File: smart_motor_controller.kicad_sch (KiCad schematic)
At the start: 35 parts, among them J10 USB_B_Micro, J101 Breakout, J102 I2C_CONN, J103 CAN_CONN, J104 Debug, J9 Input 12V, SW102 SW_NRST, SW103 SW_NRST, U2 STM32F405RGT6, U3 USBLC6-2SC6

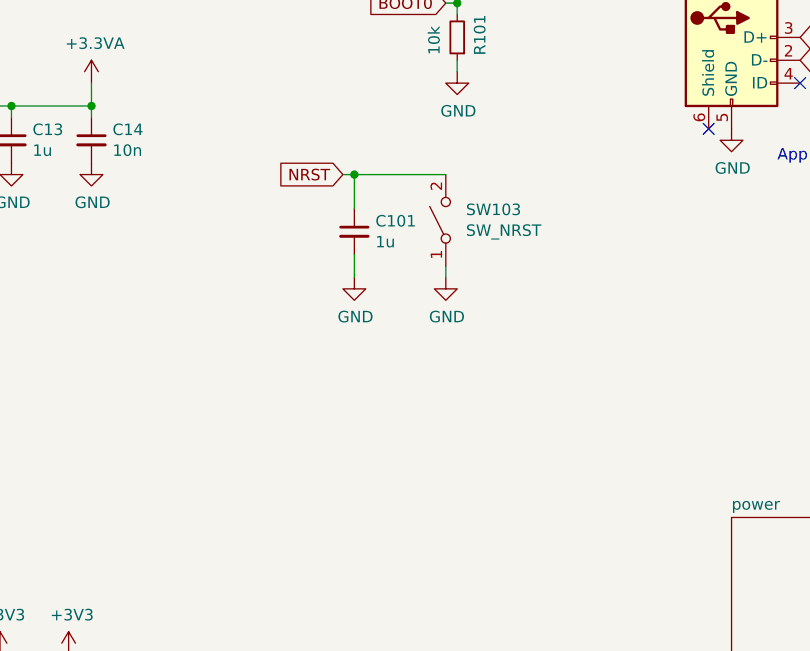
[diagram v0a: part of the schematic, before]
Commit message: Change components to 0603
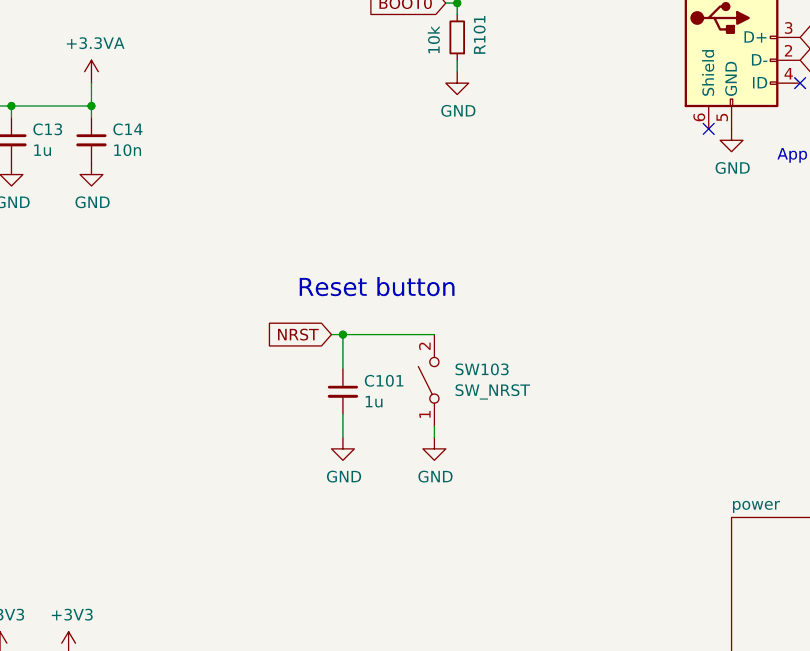
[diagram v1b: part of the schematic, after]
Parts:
- C101, C13, C14, C17, C18, C5, C6, C7, C8: footprint Capacitor_SMD:C_0402_1005Metric -> Capacitor_SMD:C_0603_1608Metric
- L2: footprint Inductor_SMD:L_0402_1005Metric -> Inductor_SMD:L_0603_1608Metric
- R101, R14, R15, R6: footprint Resistor_SMD:R_0402_1005Metric -> Resistor_SMD:R_0603_1608Metric
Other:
- note added: "Reset button"
- moved on the sheet: C101, SW103

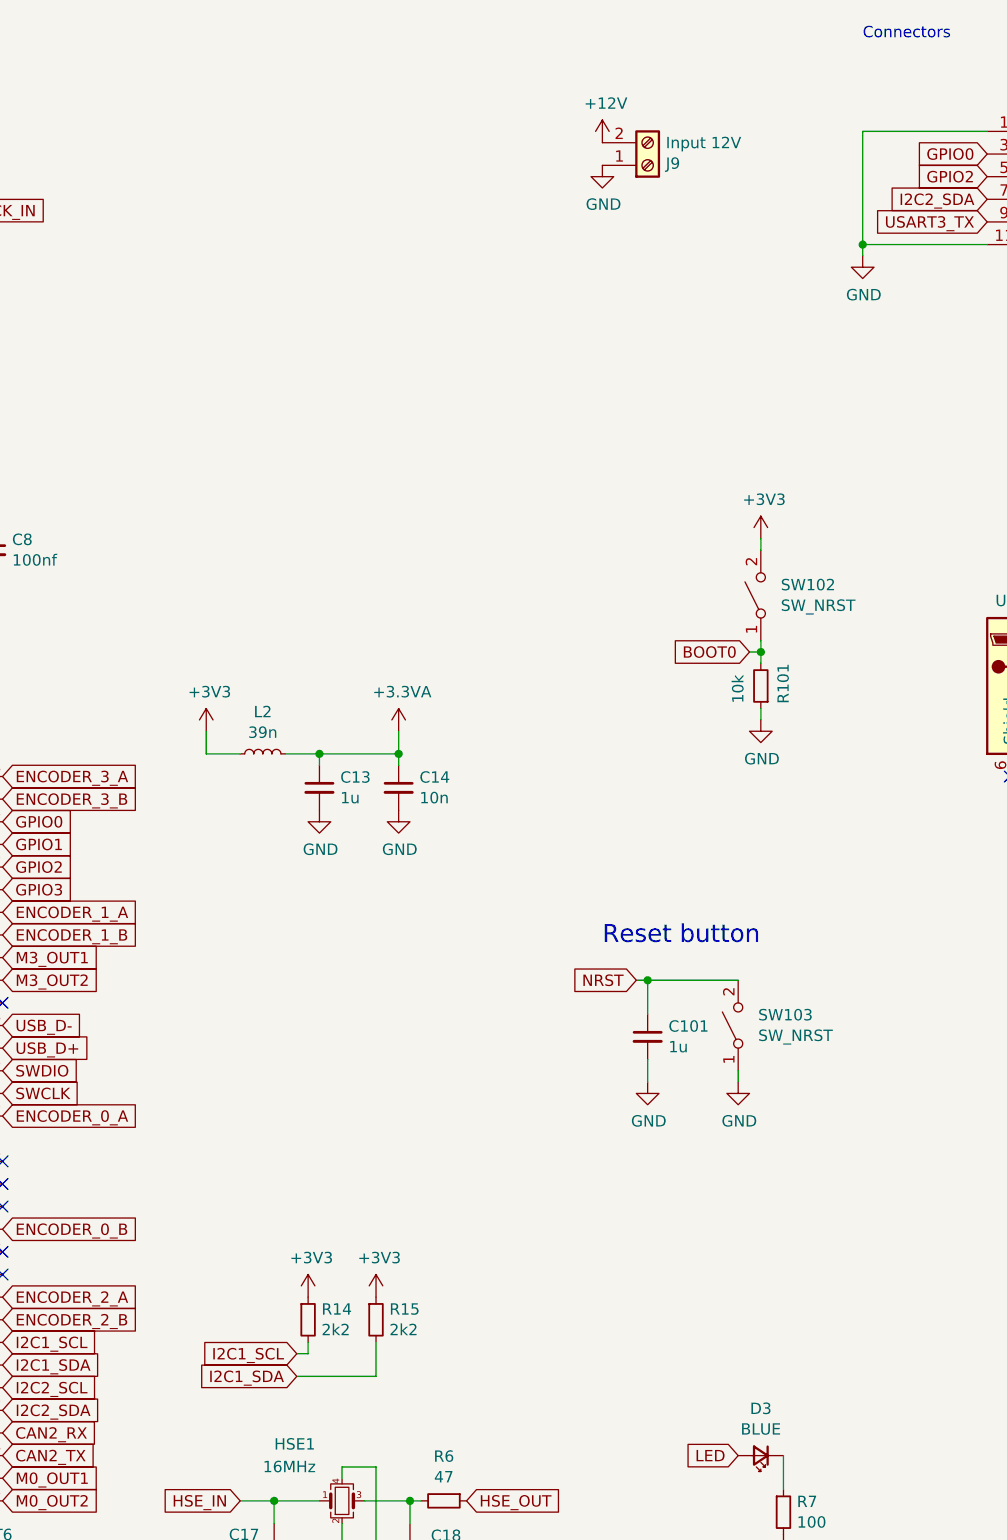
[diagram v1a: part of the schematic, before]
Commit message: Reorganized motor drivers
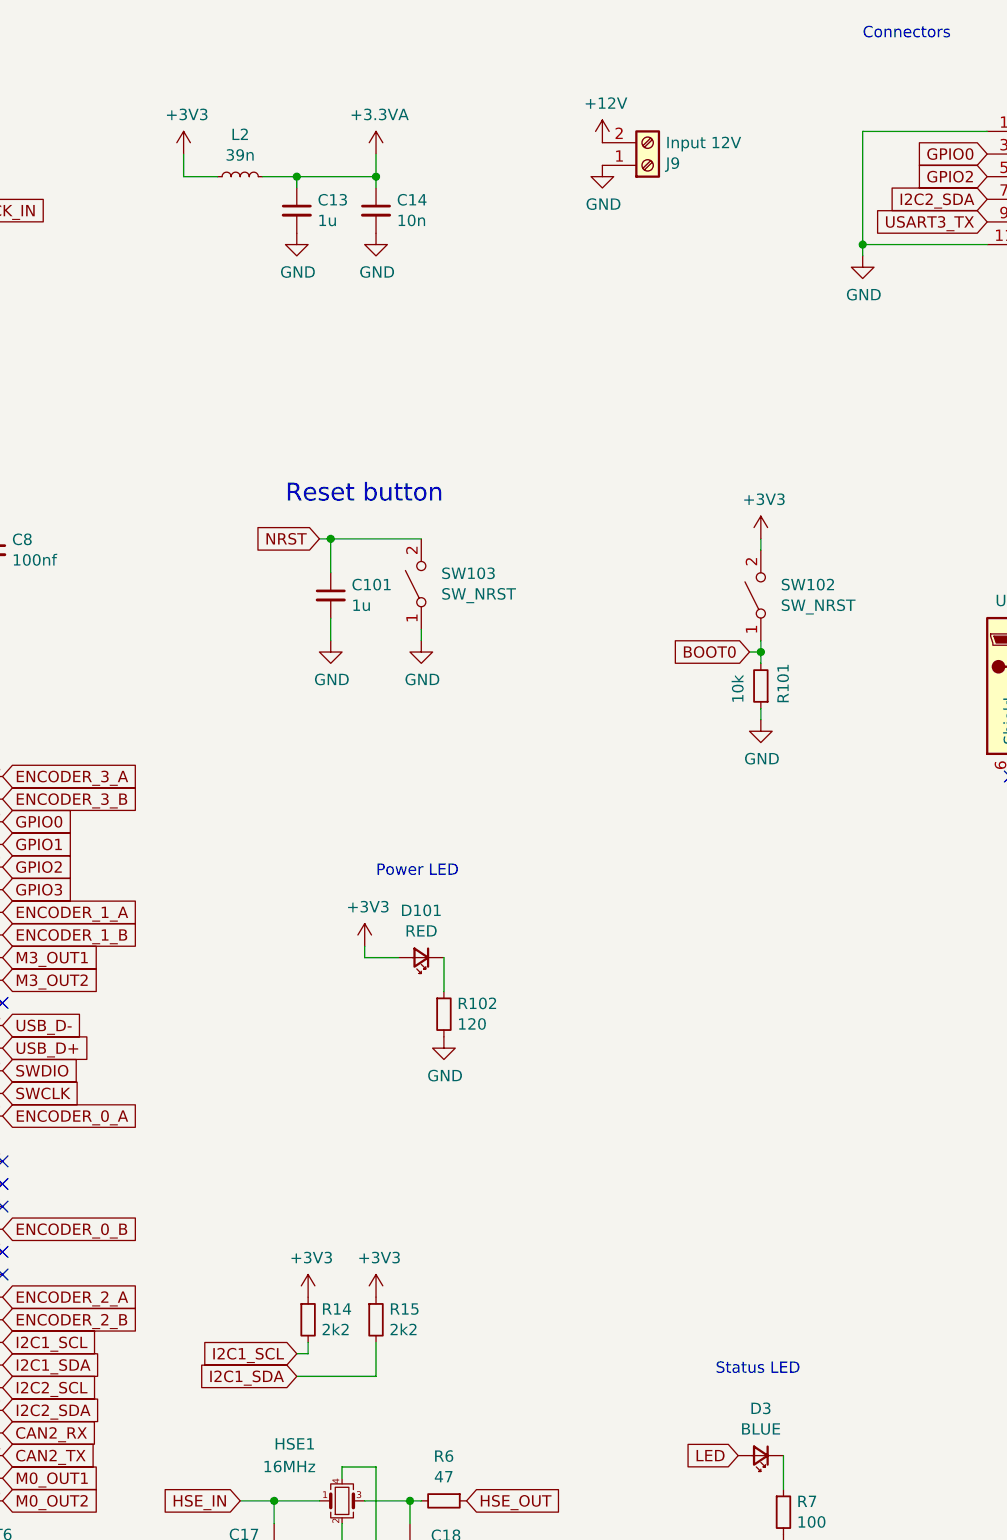
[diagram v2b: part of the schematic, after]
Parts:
- added D101: RED, LED_SMD:LED_0603_1608Metric, symbol Device:LED_Small
- added R102: 120, Resistor_SMD:R_0603_1608Metric, symbol Device:R_Small
- C4: footprint Capacitor_SMD:C_0402_1005Metric -> Capacitor_SMD:C_0603_1608Metric
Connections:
- net +3V3: now also D101.2 (A)
- net GND: now also R102.2
- new net: D101.1 (K), R102.1
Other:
- note added: "Power LED"
- note added: "Status LED"
- moved on the sheet: C101, C13, C14, L2, SW103

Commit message: Complete layout
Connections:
- net ENCODER_0_A: now also U2.22 (PA6); no longer U2.50 (PA15)
- net ENCODER_0_B: now also U2.23 (PA7); no longer U2.55 (PB3)
- net ENCODER_1_A: now also U2.14 (PA0); no longer U2.22 (PA6)
- net ENCODER_1_B: now also U2.15 (PA1); no longer U2.23 (PA7)
- net ENCODER_3_A: now also U2.50 (PA15); no longer U2.14 (PA0)
- net ENCODER_3_B: now also U2.55 (PB3); no longer U2.15 (PA1)
- net GPIO0: now also J101.7 (Pin_7), U2.57 (PB5); no longer J101.3 (Pin_3), U2.16 (PA2)
- net GPIO1: now also J101.8 (Pin_8), U2.56 (PB4); no longer J101.4 (Pin_4), U2.17 (PA3)
- net GPIO2: now also U2.54 (PD2); no longer U2.20 (PA4)
- net GPIO3: now also U2.53 (PC12); no longer U2.21 (PA5)
- net I2C1_SCL: now also J101.10 (Pin_10); no longer J102.2 (Pin_2), R14.2
- net I2C1_SDA: now also J101.9 (Pin_9); no longer J102.3 (Pin_3), R15.2
- net I2C2_SCL: now also J102.2 (Pin_2), R14.2; no longer J101.8 (Pin_8)
- net I2C2_SDA: now also J102.3 (Pin_3), R15.2; no longer J101.7 (Pin_7)
- net LED: now also U2.16 (PA2); no longer U2.53 (PC12)
- net USART3_RX: now also J101.4 (Pin_4); no longer J101.10 (Pin_10)
- net USART3_TX: now also J101.3 (Pin_3); no longer J101.9 (Pin_9)
- no-connect marks 18 -> 19

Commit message: Updated gedber files
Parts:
- removed J101: Breakout, Connector_PinHeader_2.54mm:PinHeader_2x06_P2.54mm_Vertical, symbol Connector_Generic:Conn_02x06_Odd_Even
- removed J103: CAN_CONN, Connector_JST:JST_PH_B2B-PH-K_1x02_P2.00mm_Vertical, symbol smart_motor_controller-rescue:Conn_01x02_Male-Connector
- added J101: Conn_02x07_Odd_Even, Connector_PinHeader_2.54mm:PinHeader_2x07_P2.54mm_Vertical, symbol Connector_Generic:Conn_02x07_Odd_Even
- added R103, R104: 15, Resistor_SMD:R_0603_1608Metric, symbol Device:R_Small
- C101, C13: LCSC Part # C52923 -> C2857982
- C14: value 10n -> 10nf; LCSC Part # C15195 -> C915831
- C17, C18: LCSC Part # C1547 -> C1642
- C4, C5, C6, C7, C8: LCSC Part # C1525 -> C694249
- L2: LCSC Part # C26443 -> C964035
- R101: value 10k -> 10K; LCSC Part # C25744 -> C116677
- R102: LCSC Part # C22775 -> C3016243
- R14, R15: LCSC Part # C25879 -> C328351
- R6: LCSC Part # C25118 -> C1211
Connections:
- net +3V3: now also J101.14 (Pin_14), J101.2 (Pin_2)
- net CAN2_RX: now also J101.4 (Pin_4)
- net CAN2_TX: now also J101.3 (Pin_3)
- net GND: now also J10.6 (Shield), J101.1 (Pin_1), J101.13 (Pin_13)
- net GPIO0: now also J101.9 (Pin_9)
- net GPIO1: now also J101.10 (Pin_10)
- net GPIO2: now also J101.7 (Pin_7)
- net GPIO3: now also J101.8 (Pin_8)
- net I2C1_SCL: now also J101.12 (Pin_12)
- net I2C1_SDA: now also J101.11 (Pin_11)
- net USART3_RX: now also J101.6 (Pin_6)
- net USART3_TX: now also J101.5 (Pin_5)
- net USB_D+: now also R104.1; no longer U3.4 (I/O2)
- net USB_D-: now also R103.2; no longer U3.6 (I/O1)
- new net: R104.2, U3.4 (I/O2)
- new net: R103.1, U3.6 (I/O1)
- no-connect marks 19 -> 18
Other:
- note added: "BOOT button"
- note added: "POWER"
- moved on the sheet: J10, TP2, U3

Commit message: Add CLAUDE.md for repository guidance and design documentation
- Introduced CLAUDE.md to provide an overview of the Kinisi smart motor controller board design.
- Included details on editing design files, fabrication workflow for JLCPCB, and revision management.
- Documented companion repositories for firmware and client libraries.
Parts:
- C101, C13: LCSC Part # C2857982 -> C15849
- C14: LCSC Part # C915831 -> C57112
- D3: LCSC Part # C72041 -> C193191
- R102: LCSC Part # C3016243 -> C22787
- R14, R15: LCSC Part # C328351 -> C4190
